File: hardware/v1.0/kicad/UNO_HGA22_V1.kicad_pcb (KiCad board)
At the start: 2 copper layers, 35.6 x 53.3 mm, 63 parts, among them J1 Power, J3 Analog, J4 Digital/PWM, Q1 BSS138, U1 LM321LV, U2 LM321LV, U3 LP5907MFX-3.3, U4 LP5907MFX-4.5

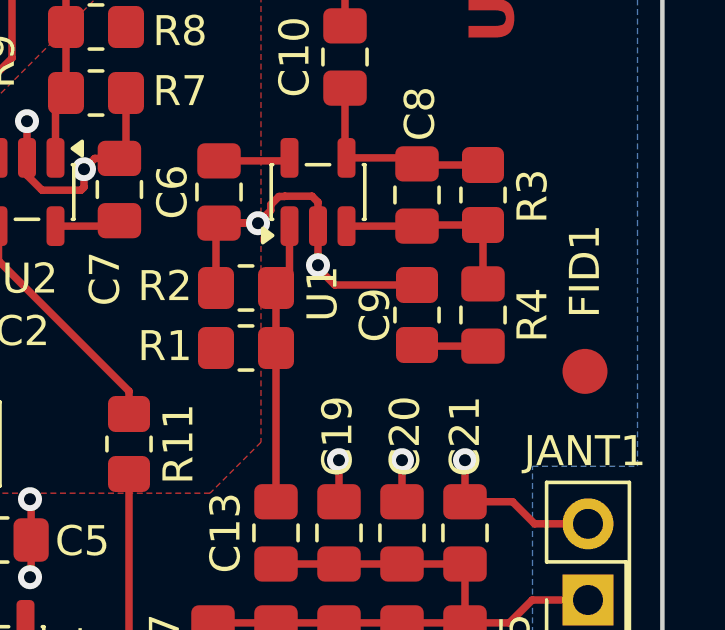
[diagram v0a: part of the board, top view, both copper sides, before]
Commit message: Update HW Documentation. Fixing Schematic and PCB Silkscreen. Added generated Interactive BOM.
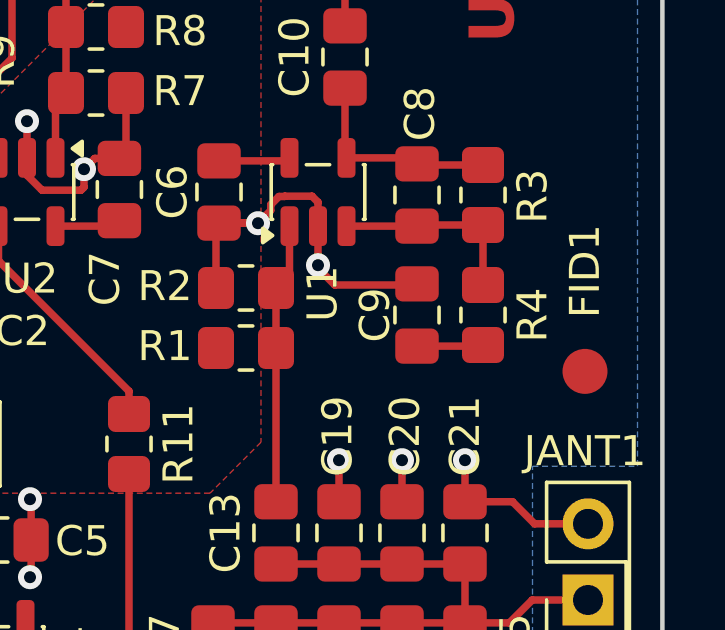
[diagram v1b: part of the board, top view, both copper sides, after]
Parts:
- R10: value 100k/1% -> 1M/1%
- R14, R4: value 100/1% -> 1k/1%
- R15: value 100/1% -> 10k/1%
- R16: value 100/1% -> 100k/1%
- R3: value 1M/1% -> 30k/1%
- R7: renamed from R8; value 330k/1% -> 1M/1%
- U1: value LM321LV -> MCP6476U
- moved C9 2.20 mm to (160.4, 77.8), turned to -90 degrees
- moved R4 2.20 mm to (162.6, 77.8), turned to 90 degrees
- renumbered R7 to R8
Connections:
- C9 pad 1: Net-(C9-Pad1) -> GND
- C9 pad 2: Net-(U1--) -> Net-(C9-Pad2)
- R4 pad 1: GND -> Net-(C9-Pad2)
- R4 pad 2: Net-(C9-Pad1) -> Net-(U1--)
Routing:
- net Net-(C9-Pad2): track 0.00 -> 2.22 mm
- net Net-(C9-Pad1): track 2.22 -> 0.00 mm
